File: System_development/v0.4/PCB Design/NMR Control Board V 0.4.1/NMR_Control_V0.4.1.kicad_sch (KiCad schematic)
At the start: 49 parts, among them J1 Conn_Coaxial, J2 Pin Hole, U1 LM7812_TO220, U2 NCP1117-5.0_TO252, U3 LM828M5

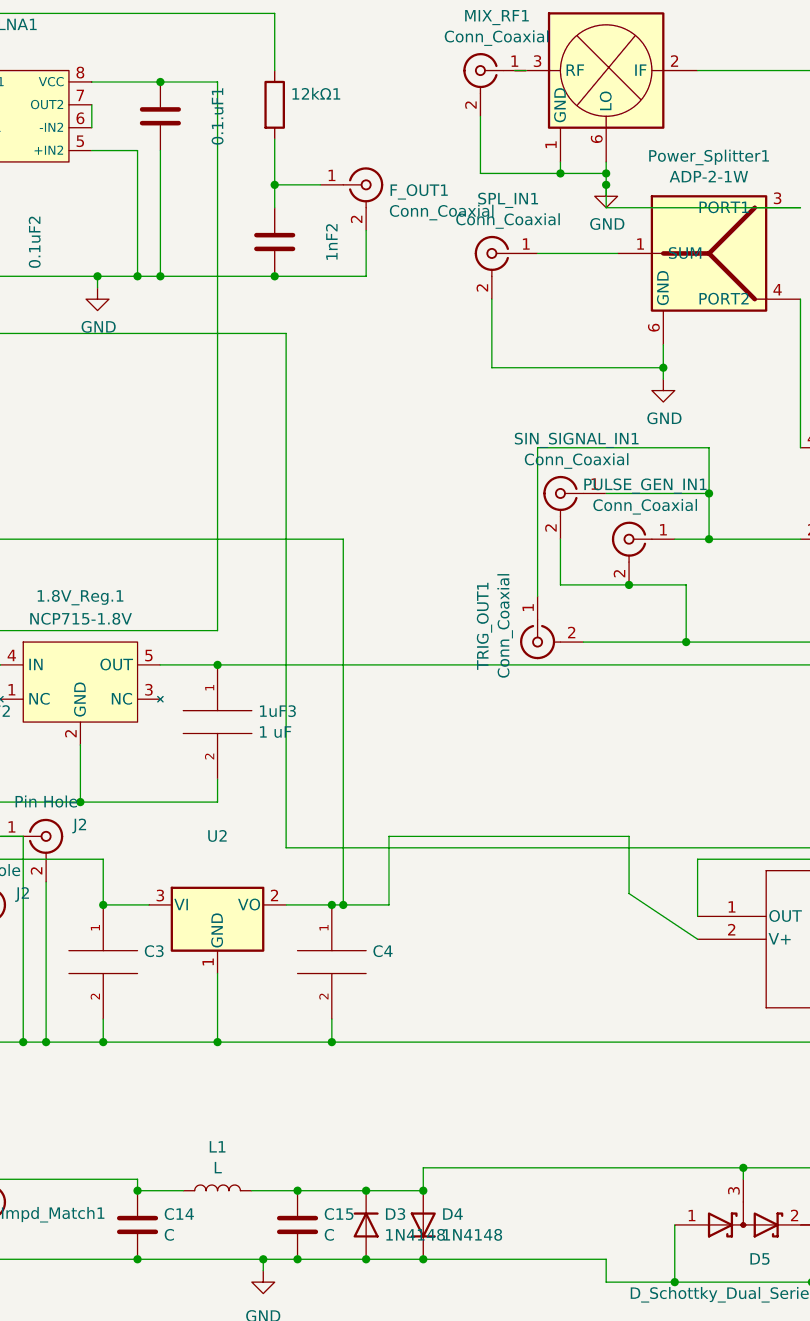
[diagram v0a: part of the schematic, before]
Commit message: Control Board 0.4.1 adjustments
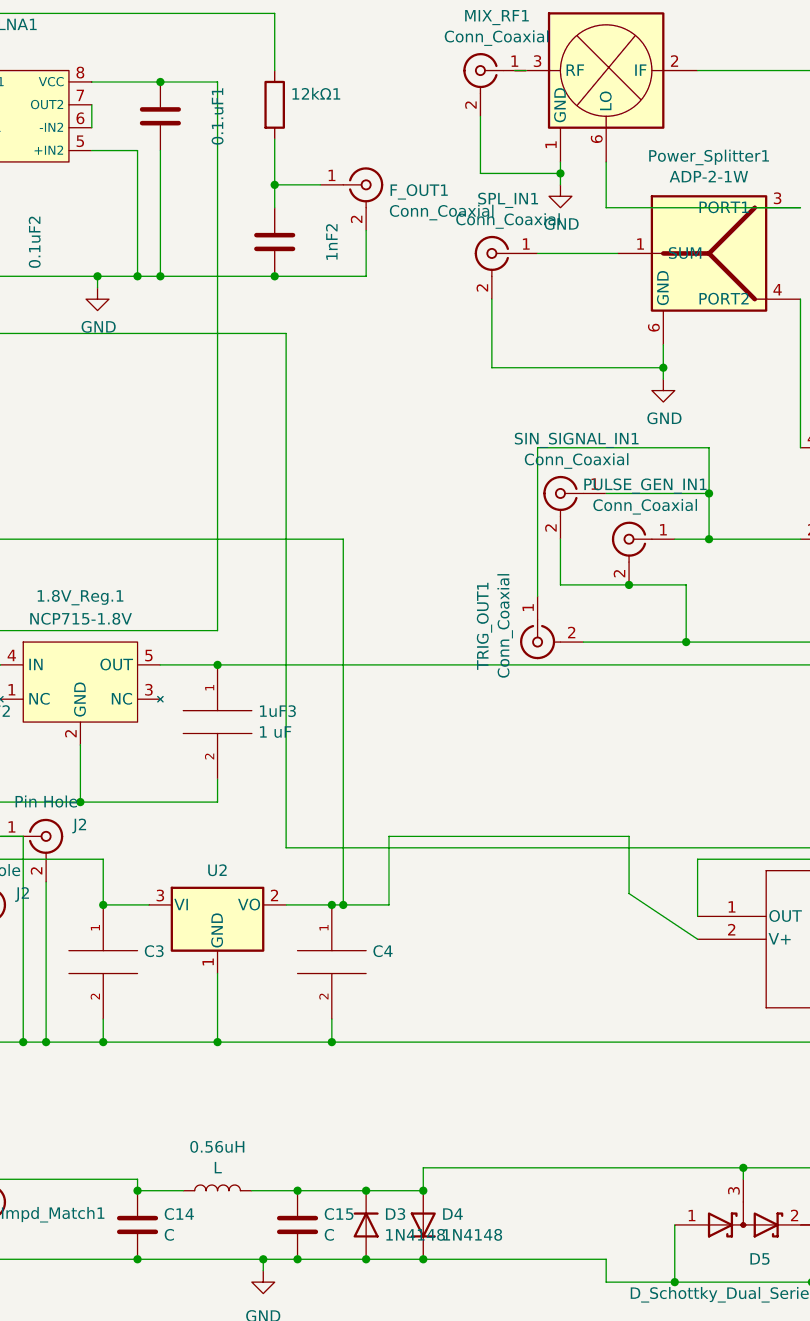
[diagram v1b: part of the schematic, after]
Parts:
- C3: footprint Capacitor_SMD:C_0805_2012Metric -> Capacitor_SMD:C_1206_3216Metric_Pad1.33x1.80mm_HandSolder
- C4: footprint Capacitor_SMD:C_0805_2012Metric -> Capacitor_SMD:C_1206_3216Metric
- renumbered L1 to 0.56uH
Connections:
- net GND: no longer Mixer1.6 (LO), Power_Splitter1.3 (PORT1)
- new net: Mixer1.6 (LO), Power_Splitter1.3 (PORT1)
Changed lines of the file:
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@@
   (junction (at 190.5 158.75) (diameter 0) (color 0 0 0 0)
   )
-  (junction (at 147.32 49.53) (diameter 0) (color 0 0 0 0)
-  )
   (junction (at 182.88 171.45) (diameter 0) (color 0 0 0 0)
   )
@@
   (junction (at 127 168.91) (diameter 0) (color 0 0 0 0)
   )
-  (junction (at 147.32 48.26) (diameter 0) (color 0 0 0 0)
-  )
   (junction (at 60.96 102.87) (diameter 0) (color 0 0 0 0)
   )
@@
     (stroke (width 0) (type default))
   )
+  (wire (pts (xy 142.24 48.26) (xy 142.24 49.53))
+    (stroke (width 0) (type default))
+  )
   (wire (pts (xy 139.7 95.25) (xy 139.7 78.74))
     (stroke (width 0) (type default))
@@
     (stroke (width 0) (type default))
   )
-  (wire (pts (xy 147.32 48.26) (xy 147.32 46.99))
-    (stroke (width 0) (type default))
-  )
   (wire (pts (xy 78.74 144.78) (xy 82.55 144.78))
     (stroke (width 0) (type default))
@@
     (stroke (width 0) (type default))
   )
-  (wire (pts (xy 147.32 52.07) (xy 147.32 49.53))
+  (wire (pts (xy 147.32 46.99) (xy 147.32 52.07))
     (stroke (width 0) (type default))
   )
@@
     (stroke (width 0) (type default))
   )
-  (wire (pts (xy 147.32 48.26) (xy 147.32 49.53))
-    (stroke (width 0) (type default))
-  )
   (wire (pts (xy 237.49 123.19) (xy 237.49 124.46))
     (stroke (width 0) (type default))
@@
   )
   (wire (pts (xy 182.88 165.1) (xy 182.88 171.45))
-    (stroke (width 0) (type default))
-  )
-  (wire (pts (xy 142.24 48.26) (xy 147.32 48.26))
     (stroke (width 0) (type default))
   )
@@
       (effects (font (size 1.27 1.27)) (justify left) hide)
     )
-    (property "Footprint" "Capacitor_SMD:C_0805_2012Metric" (at 116.84 135.89 0)
+    (property "Footprint" "Capacitor_SMD:C_1206_3216Metric" (at 116.84 135.89 0)
       (effects (font (size 1.27 1.27)) hide)
     )
@@
       (effects (font (size 1.27 1.27)) (justify left) hide)
     )
-    (property "Footprint" "Capacitor_SMD:C_0805_2012Metric" (at 91.44 135.89 0)
+    (property "Footprint" "Capacitor_SMD:C_1206_3216Metric_Pad1.33x1.80mm_HandSolder" (at 91.44 135.89 0)
       (effects (font (size 1.27 1.27)) hide)
     )
@@
     )
   )
-  (symbol (lib_id "power:GND") (at 147.32 49.53 0) (unit 1)
-    (in_bom yes) (on_board yes) (dnp no)
-    (property "Reference" "#PWR0103" (at 147.32 55.88 0)
-      (effects (font (size 1.27 1.27)) hide)
-    )
-    (property "Value" "GND" (at 147.447 53.9242 0)
-      (effects (font (size 1.27 1.27)))
-    )
-    (property "Footprint" "" (at 147.32 49.53 0)
-      (effects (font (size 1.27 1.27)) hide)
-    )
-    (property "Datasheet" "" (at 147.32 49.53 0)
+  (symbol (lib_id "power:GND") (at 142.24 49.53 0) (unit 1)
+    (in_bom yes) (on_board yes) (dnp no)
+    (property "Reference" "#PWR0103" (at 142.24 55.88 0)
+      (effects (font (size 1.27 1.27)) hide)
+    )
+    (property "Value" "GND" (at 142.367 53.9242 0)
+      (effects (font (size 1.27 1.27)))
+    )
+    (property "Footprint" "" (at 142.24 49.53 0)
+      (effects (font (size 1.27 1.27)) hide)
+    )
+    (property "Datasheet" "" (at 142.24 49.53 0)
       (effects (font (size 1.27 1.27)) hide)
     )
@@
   (symbol (lib_id "Regulator_Linear:NCP1117-5.0_TO252") (at 104.14 129.54 0) (unit 1)
     (in_bom yes) (on_board yes) (dnp no) (fields_autoplaced)
-    (property "Reference" "U2" (at 104.14 121.92 0)
+    (property "Reference" "U2" (at 104.14 125.73 0)
       (effects (font (size 1.27 1.27)))
     )
@@
       (project "NMR main Board"
         (path "/9a38510c-4adf-4cce-9077-4bd61adcc8bf"
-          (reference "6V_REG1") (unit 1)
+          (reference "5V_REG1") (unit 1)
         )
       )
@@
   (symbol (lib_id "Device:L") (at 104.14 161.29 90) (unit 1)
     (in_bom yes) (on_board yes) (dnp no)
-    (property "Reference" "L1" (at 104.14 156.464 90)
+    (property "Reference" "0.56uH" (at 104.14 156.464 90)
       (effects (font (size 1.27 1.27)))
     )
@@
       (project "NMR main Board"
         (path "/9a38510c-4adf-4cce-9077-4bd61adcc8bf"
-          (reference "L1") (unit 1)
-        )
-      )
+          (reference "0.56uH") (unit 1)
+        )
+      )
